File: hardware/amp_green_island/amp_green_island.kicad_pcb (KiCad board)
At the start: 4 copper layers, 100 x 100 mm, 39 parts, among them J501 input, J502 output, J503 Conn_01x04_Pin, U101 OP27, U102 TL072

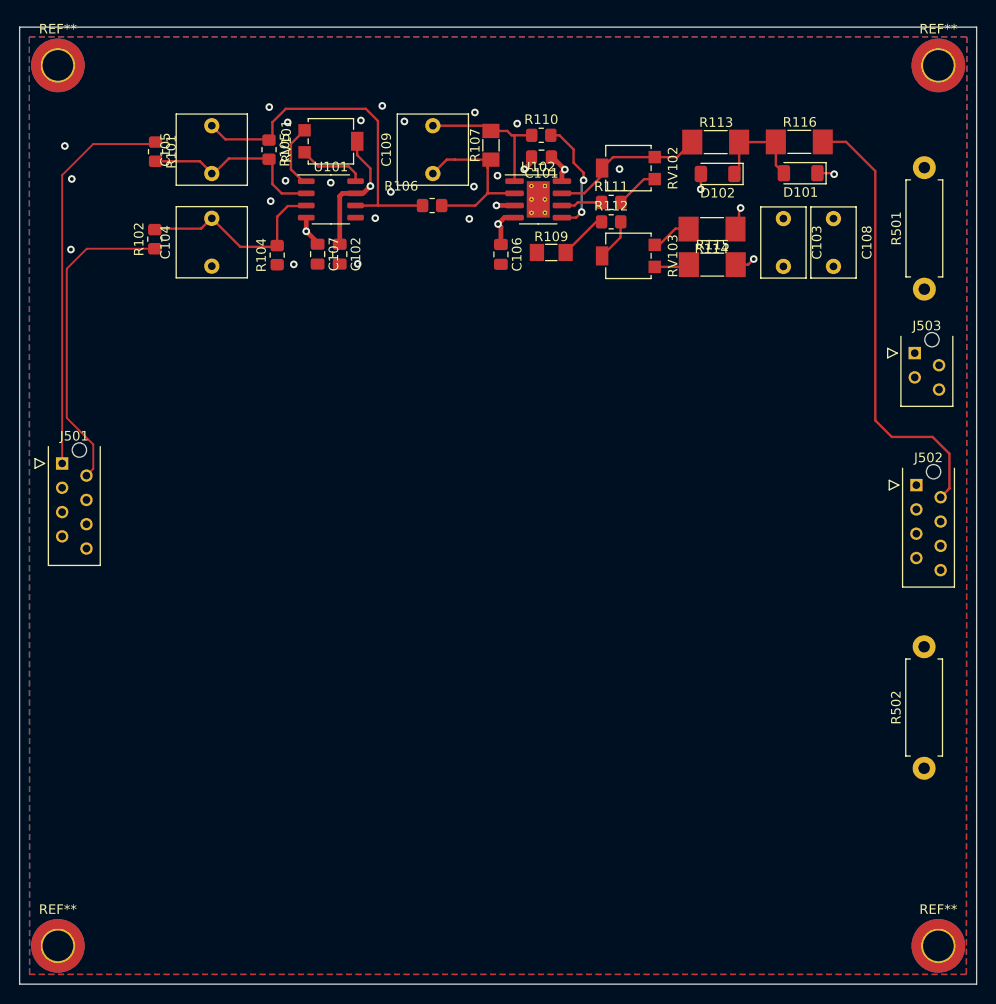
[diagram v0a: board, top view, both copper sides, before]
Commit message: amp_green_island: add all 4 channels to schematic
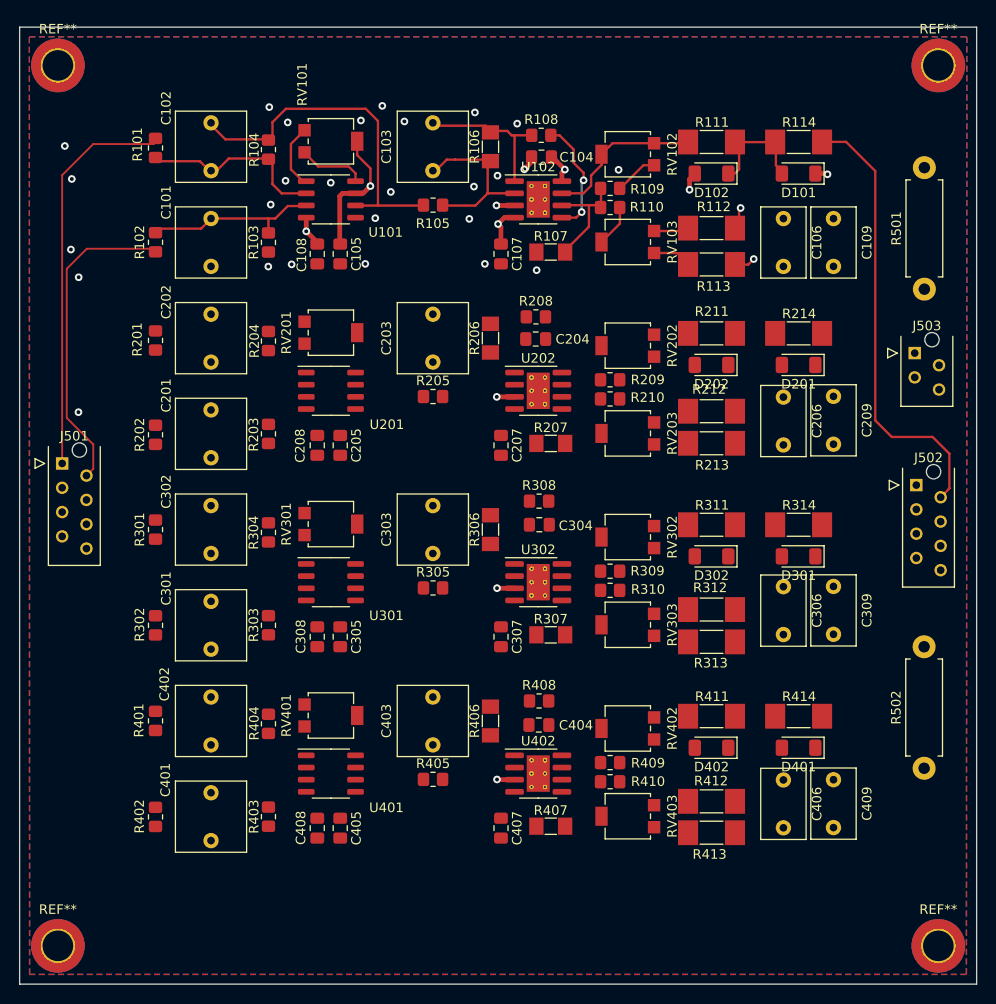
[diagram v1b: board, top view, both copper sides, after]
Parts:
- added C201: 1u, Capacitor_THT:C_Rect_L7.2mm_W7.2mm_P5.00mm_FKS2_FKP2_MKS2_MKP2, F.Cu at (120.0, 95.0)
- added C202: 1u, Capacitor_THT:C_Rect_L7.2mm_W7.2mm_P5.00mm_FKS2_FKP2_MKS2_MKP2, F.Cu at (120.0, 85.0)
- added C203: 1u, Capacitor_THT:C_Rect_L7.2mm_W7.2mm_P5.00mm_FKS2_FKP2_MKS2_MKP2, F.Cu at (143.2, 85.0)
- added C204: 100n, Capacitor_SMD:C_0805_2012Metric_Pad1.18x1.45mm_HandSolder, F.Cu at (153.9, 82.6)
- added C205: 100n, Capacitor_SMD:C_0805_2012Metric_Pad1.18x1.45mm_HandSolder, F.Cu at (133.5, 93.7)
- added C206: 100n, Capacitor_THT:C_Rect_L7.2mm_W4.5mm_P5.00mm_FKS2_FKP2_MKS2_MKP2, F.Cu at (179.8, 88.7)
- added C207: 100n, Capacitor_SMD:C_0805_2012Metric_Pad1.18x1.45mm_HandSolder, F.Cu at (150.3, 93.7)
- added C208: 100n, Capacitor_SMD:C_0805_2012Metric_Pad1.18x1.45mm_HandSolder, F.Cu at (131.1, 93.7)
- added C209: 100n, Capacitor_THT:C_Rect_L7.2mm_W4.5mm_P5.00mm_FKS2_FKP2_MKS2_MKP2, F.Cu at (185.0, 88.6)
- added C301: 1u, Capacitor_THT:C_Rect_L7.2mm_W7.2mm_P5.00mm_FKS2_FKP2_MKS2_MKP2, F.Cu at (120.0, 115.0)
- added C302: 1u, Capacitor_THT:C_Rect_L7.2mm_W7.2mm_P5.00mm_FKS2_FKP2_MKS2_MKP2, F.Cu at (120.0, 105.0)
- added C303: 1u, Capacitor_THT:C_Rect_L7.2mm_W7.2mm_P5.00mm_FKS2_FKP2_MKS2_MKP2, F.Cu at (143.2, 105.0)
- added C304: 100n, Capacitor_SMD:C_0805_2012Metric_Pad1.18x1.45mm_HandSolder, F.Cu at (154.3, 102.0)
- added C305: 100n, Capacitor_SMD:C_0805_2012Metric_Pad1.18x1.45mm_HandSolder, F.Cu at (133.5, 113.7)
- added C306: 100n, Capacitor_THT:C_Rect_L7.2mm_W4.5mm_P5.00mm_FKS2_FKP2_MKS2_MKP2, F.Cu at (179.8, 108.5)
- added C307: 100n, Capacitor_SMD:C_0805_2012Metric_Pad1.18x1.45mm_HandSolder, F.Cu at (150.3, 113.7)
- added C308: 100n, Capacitor_SMD:C_0805_2012Metric_Pad1.18x1.45mm_HandSolder, F.Cu at (131.1, 113.7)
- added C309: 100n, Capacitor_THT:C_Rect_L7.2mm_W4.5mm_P5.00mm_FKS2_FKP2_MKS2_MKP2, F.Cu at (185.0, 108.4)
- added C401: 1u, Capacitor_THT:C_Rect_L7.2mm_W7.2mm_P5.00mm_FKS2_FKP2_MKS2_MKP2, F.Cu at (120.0, 135.0)
- added C402: 1u, Capacitor_THT:C_Rect_L7.2mm_W7.2mm_P5.00mm_FKS2_FKP2_MKS2_MKP2, F.Cu at (120.0, 125.0)
- added C403: 1u, Capacitor_THT:C_Rect_L7.2mm_W7.2mm_P5.00mm_FKS2_FKP2_MKS2_MKP2, F.Cu at (143.2, 125.0)
- added C404: 100n, Capacitor_SMD:C_0805_2012Metric_Pad1.18x1.45mm_HandSolder, F.Cu at (154.3, 122.9)
- added C405: 100n, Capacitor_SMD:C_0805_2012Metric_Pad1.18x1.45mm_HandSolder, F.Cu at (133.5, 133.7)
- added C406: 100n, Capacitor_THT:C_Rect_L7.2mm_W4.5mm_P5.00mm_FKS2_FKP2_MKS2_MKP2, F.Cu at (179.8, 128.7)
- added C407: 100n, Capacitor_SMD:C_0805_2012Metric_Pad1.18x1.45mm_HandSolder, F.Cu at (150.3, 133.7)
- added C408: 100n, Capacitor_SMD:C_0805_2012Metric_Pad1.18x1.45mm_HandSolder, F.Cu at (131.1, 133.7)
- added C409: 100n, Capacitor_THT:C_Rect_L7.2mm_W4.5mm_P5.00mm_FKS2_FKP2_MKS2_MKP2, F.Cu at (185.0, 128.6)
- added D201: LL4148, Diode_SMD:D_MiniMELF, F.Cu at (181.4, 85.3)
- added D202: LL4148, Diode_SMD:D_MiniMELF, F.Cu at (172.3, 85.3)
- added D301: LL4148, Diode_SMD:D_MiniMELF, F.Cu at (181.4, 105.3)
- added D302: LL4148, Diode_SMD:D_MiniMELF, F.Cu at (172.3, 105.3)
- added D401: LL4148, Diode_SMD:D_MiniMELF, F.Cu at (181.4, 125.3)
- added D402: LL4148, Diode_SMD:D_MiniMELF, F.Cu at (172.3, 125.3)
- added R201: 10k, Resistor_SMD:R_0805_2012Metric_Pad1.20x1.40mm_HandSolder, F.Cu at (114.2, 82.7)
- added R202: 10k, Resistor_SMD:R_0805_2012Metric_Pad1.20x1.40mm_HandSolder, F.Cu at (114.2, 92.6)
- added R203: 100k, Resistor_SMD:R_0805_2012Metric_Pad1.20x1.40mm_HandSolder, F.Cu at (126.0, 92.5)
- added R204: 100k, Resistor_SMD:R_0805_2012Metric_Pad1.20x1.40mm_HandSolder, F.Cu at (126.0, 82.8)
- added R205: 1k, Resistor_SMD:R_0805_2012Metric_Pad1.20x1.40mm_HandSolder, F.Cu at (143.2, 88.6)
- added R206: 200k, Resistor_SMD:R_MiniMELF_MMA-0204, F.Cu at (149.2, 82.5)
- added R207: 3k3, Resistor_SMD:R_MiniMELF_MMA-0204, F.Cu at (155.5, 93.5)
- added R208: 1k, Resistor_SMD:R_0805_2012Metric_Pad1.20x1.40mm_HandSolder, F.Cu at (153.9, 80.3)
- added R209: 5k6, Resistor_SMD:R_0805_2012Metric_Pad1.20x1.40mm_HandSolder, F.Cu at (161.7, 86.8)
- added R210: 82k, Resistor_SMD:R_0805_2012Metric_Pad1.20x1.40mm_HandSolder, F.Cu at (161.7, 88.8)
- added R211: 470, Resistor_SMD:R_MELF_MMB-0207, F.Cu at (172.3, 82.0)
- added R212: 33k, Resistor_SMD:R_MELF_MMB-0207, F.Cu at (172.3, 90.1)
- added R213: 33k, Resistor_SMD:R_MELF_MMB-0207, F.Cu at (172.3, 93.5)
- added R214: 470, Resistor_SMD:R_MELF_MMB-0207, F.Cu at (181.4, 82.0)
- added R301: 10k, Resistor_SMD:R_0805_2012Metric_Pad1.20x1.40mm_HandSolder, F.Cu at (114.2, 102.5)
- added R302: 10k, Resistor_SMD:R_0805_2012Metric_Pad1.20x1.40mm_HandSolder, F.Cu at (114.2, 112.5)
- added R303: 100k, Resistor_SMD:R_0805_2012Metric_Pad1.20x1.40mm_HandSolder, F.Cu at (126.0, 112.5)
- added R304: 100k, Resistor_SMD:R_0805_2012Metric_Pad1.20x1.40mm_HandSolder, F.Cu at (126.0, 102.8)
- added R305: 1k, Resistor_SMD:R_0805_2012Metric_Pad1.20x1.40mm_HandSolder, F.Cu at (143.2, 108.6)
- added R306: 200k, Resistor_SMD:R_MiniMELF_MMA-0204, F.Cu at (149.2, 102.5)
- added R307: 3k3, Resistor_SMD:R_MiniMELF_MMA-0204, F.Cu at (155.5, 113.5)
- added R308: 1k, Resistor_SMD:R_0805_2012Metric_Pad1.20x1.40mm_HandSolder, F.Cu at (154.3, 99.5)
- added R309: 5k6, Resistor_SMD:R_0805_2012Metric_Pad1.20x1.40mm_HandSolder, F.Cu at (161.7, 106.8)
- added R310: 82k, Resistor_SMD:R_0805_2012Metric_Pad1.20x1.40mm_HandSolder, F.Cu at (161.7, 108.8)
- added R311: 470, Resistor_SMD:R_MELF_MMB-0207, F.Cu at (172.3, 102.0)
- added R312: 33k, Resistor_SMD:R_MELF_MMB-0207, F.Cu at (172.3, 110.9)
- added R313: 33k, Resistor_SMD:R_MELF_MMB-0207, F.Cu at (172.3, 114.2)
- added R314: 470, Resistor_SMD:R_MELF_MMB-0207, F.Cu at (181.4, 102.0)
- added R401: 10k, Resistor_SMD:R_0805_2012Metric_Pad1.20x1.40mm_HandSolder, F.Cu at (114.2, 122.5)
- added R402: 10k, Resistor_SMD:R_0805_2012Metric_Pad1.20x1.40mm_HandSolder, F.Cu at (114.2, 132.5)
- added R403: 100k, Resistor_SMD:R_0805_2012Metric_Pad1.20x1.40mm_HandSolder, F.Cu at (126.0, 132.5)
- added R404: 100k, Resistor_SMD:R_0805_2012Metric_Pad1.20x1.40mm_HandSolder, F.Cu at (126.0, 122.8)
- added R405: 1k, Resistor_SMD:R_0805_2012Metric_Pad1.20x1.40mm_HandSolder, F.Cu at (143.2, 128.6)
- added R406: 200k, Resistor_SMD:R_MiniMELF_MMA-0204, F.Cu at (149.2, 122.5)
- added R407: 3k3, Resistor_SMD:R_MiniMELF_MMA-0204, F.Cu at (155.5, 133.5)
- added R408: 1k, Resistor_SMD:R_0805_2012Metric_Pad1.20x1.40mm_HandSolder, F.Cu at (154.3, 120.4)
- added R409: 5k6, Resistor_SMD:R_0805_2012Metric_Pad1.20x1.40mm_HandSolder, F.Cu at (161.7, 126.8)
- added R410: 82k, Resistor_SMD:R_0805_2012Metric_Pad1.20x1.40mm_HandSolder, F.Cu at (161.7, 128.8)
- added R411: 470, Resistor_SMD:R_MELF_MMB-0207, F.Cu at (172.3, 122.0)
- added R412: 33k, Resistor_SMD:R_MELF_MMB-0207, F.Cu at (172.3, 130.9)
- added R413: 33k, Resistor_SMD:R_MELF_MMB-0207, F.Cu at (172.3, 134.2)
- added R414: 470, Resistor_SMD:R_MELF_MMB-0207, F.Cu at (181.4, 122.0)
- added RV201: 10k, Potentiometer_SMD:Potentiometer_Bourns_3314G_Vertical, F.Cu at (132.5, 81.9)
- added RV202: 50k, Potentiometer_SMD:Potentiometer_Bourns_3314G_Vertical, F.Cu at (163.6, 83.3)
- added RV203: 5k, Potentiometer_SMD:Potentiometer_Bourns_3314G_Vertical, F.Cu at (163.6, 92.5)
- added RV301: 10k, Potentiometer_SMD:Potentiometer_Bourns_3314G_Vertical, F.Cu at (132.5, 101.9)
- added RV302: 50k, Potentiometer_SMD:Potentiometer_Bourns_3314G_Vertical, F.Cu at (163.6, 103.3)
- added RV303: 5k, Potentiometer_SMD:Potentiometer_Bourns_3314G_Vertical, F.Cu at (163.6, 112.5)
- added RV401: 10k, Potentiometer_SMD:Potentiometer_Bourns_3314G_Vertical, F.Cu at (132.5, 121.9)
- added RV402: 50k, Potentiometer_SMD:Potentiometer_Bourns_3314G_Vertical, F.Cu at (163.6, 123.3)
- added RV403: 5k, Potentiometer_SMD:Potentiometer_Bourns_3314G_Vertical, F.Cu at (163.6, 132.5)
- added U201: OP27, Package_SO:SO-8_3.9x4.9mm_P1.27mm, F.Cu at (132.5, 88.0)
- added U202: TL072, Package_SO:SOIC-8-1EP_3.9x4.9mm_P1.27mm_EP2.41x3.81mm_ThermalVias, F.Cu at (154.2, 88.0)
- added U301: OP27, Package_SO:SO-8_3.9x4.9mm_P1.27mm, F.Cu at (132.5, 108.0)
- added U302: TL072, Package_SO:SOIC-8-1EP_3.9x4.9mm_P1.27mm_EP2.41x3.81mm_ThermalVias, F.Cu at (154.2, 108.0)
- added U401: OP27, Package_SO:SO-8_3.9x4.9mm_P1.27mm, F.Cu at (132.5, 128.0)
- added U402: TL072, Package_SO:SOIC-8-1EP_3.9x4.9mm_P1.27mm_EP2.41x3.81mm_ThermalVias, F.Cu at (154.2, 128.0)
- moved R103 1.61 mm to (126.0, 72.5)
- moved R110 1.50 mm to (161.7, 68.8)
- moved R109 1.47 mm to (161.7, 66.8)
- moved RV102 1.45 mm to (163.6, 63.3)
- moved RV103 1.45 mm to (163.6, 72.5)
- moved D102 0.64 mm to (172.3, 65.3)
- moved R111 0.44 mm to (172.3, 62.0)
- moved R101 0.39 mm to (114.2, 62.6)
- moved R102 0.33 mm to (114.2, 72.5)
- moved C102 0.31 mm to (120.0, 65.0)
- moved C103 0.30 mm to (143.2, 65.0)
- moved D101 0.21 mm to (181.4, 65.3)
- moved R106 0.16 mm to (149.2, 62.5)
- moved R112 0.12 mm to (172.3, 71.0)
- moved R105 0.11 mm to (143.2, 68.6)
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- renumbered C104 to C101, C105 to C102, C109 to C103, C101 to C104, C102 to C105, C103 to C106, C106 to C107, C107 to C108, C108 to C109, R104 to R103, R105 to R104, R106 to R105, R107 to R106, R109 to R107, R110 to R108, R111 to R109, R112 to R110, R113 to R111, R114 to R112, R115 to R113, R116 to R114
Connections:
- J501 pad 3: unconnected-(J501-Pin_3-Pad3) -> in2_-
- J501 pad 4: unconnected-(J501-Pin_4-Pad4) -> in2_+
- J501 pad 5: unconnected-(J501-Pin_5-Pad5) -> in3_-
- J501 pad 6: unconnected-(J501-Pin_6-Pad6) -> in3_+
- J501 pad 7: unconnected-(J501-Pin_7-Pad7) -> in4_-
- J501 pad 8: unconnected-(J501-Pin_8-Pad8) -> in4_+
- J502 pad 4: unconnected-(J502-Pin_4-Pad4) -> out2
- J502 pad 6: unconnected-(J502-Pin_6-Pad6) -> out3
- J502 pad 8: unconnected-(J502-Pin_8-Pad8) -> out4
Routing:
- net GND: track 3.77 -> 9.30 mm, vias 23 -> 31
- net Net-(U102B--): track 9.36 -> 12.2 mm
- net Net-(U101-+): track 21.1 -> 18.4 mm
- net Net-(R112-Pad2): track 4.61 -> 3.68 mm
- net Net-(R111-Pad1): track 16.3 -> 17.1 mm
- net -12V: track 131.1 -> 131.8 mm

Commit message: green_island: pcb routing done
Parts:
- added C501: 220u, Capacitor_SMD:C_Elec_8x10.2, F.Cu at (163.8, 142.3)
- added C502: 220u, Capacitor_SMD:C_Elec_8x10.2, F.Cu at (182.5, 142.3)
- moved J502 2.46 mm to (193.7, 95.4)
- moved R308 1.78 mm to (154.5, 101.3)
- moved C304 1.62 mm to (154.5, 103.6), turned to 180 degrees
- moved C309 1.55 mm to (185.0, 110.0)
- moved C306 1.53 mm to (179.8, 110.0)
- moved C209 1.42 mm to (185.0, 90.0)
- moved C409 1.36 mm to (185.0, 130.0)
- moved C206 1.34 mm to (179.8, 90.0)
- moved C406 1.34 mm to (179.8, 130.0)
- moved R213 1.32 mm to (172.3, 94.8)
- moved C204 1.16 mm to (154.5, 83.6), turned to 180 degrees
- moved R208 1.16 mm to (154.5, 81.3)
- moved R408 0.92 mm to (154.5, 121.3)
- moved R212 0.87 mm to (172.3, 91.0)
- moved C404 0.72 mm to (154.5, 123.6), turned to 180 degrees
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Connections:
- J502 pad 1: GND -> out1
- J502 pad 2: out1 -> GND
- J502 pad 3: GND -> out2
- J502 pad 4: out2 -> GND
- J502 pad 5: GND -> out3
- J502 pad 6: out3 -> GND
- J502 pad 7: GND -> out4
- J502 pad 8: out4 -> GND
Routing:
- net +12V: track 119.1 -> 472.2 mm, vias 4 -> 18
- net -12V: track 131.8 -> 473.0 mm, vias 4 -> 18
- net Net-(C202-Pad2): track 0.00 -> 37.8 mm
- net Net-(C302-Pad2): track 0.00 -> 37.4 mm
- net Net-(C402-Pad2): track 0.00 -> 37.1 mm
- net in4_+: track 0.00 -> 31.8 mm
- net in2_-: track 0.00 -> 27.1 mm
- net in4_-: track 0.00 -> 25.7 mm
- net out4: track 0.00 -> 25.4 mm
- net out2: track 0.00 -> 20.6 mm
- net Net-(U301--): track 0.00 -> 20.6 mm
- net Net-(U201--): track 0.00 -> 19.9 mm
- net Net-(U401--): track 0.00 -> 19.7 mm
- net Net-(U301-+): track 0.00 -> 19.6 mm
- net Net-(U401-+): track 0.00 -> 19.3 mm
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- added copper zone on In2.Cu, net GND

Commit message: amp_green_island: pcb verified
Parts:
- added D501: LED, LED_SMD:LED_0805_2012Metric_Pad1.15x1.40mm_HandSolder, F.Cu at (118.7, 145.7)
- added D502: LED, LED_SMD:LED_0805_2012Metric_Pad1.15x1.40mm_HandSolder, F.Cu at (113.9, 145.7)
- added R503: 100k, Resistor_SMD:R_0805_2012Metric_Pad1.20x1.40mm_HandSolder, F.Cu at (118.7, 142.1)
- added R504: 100k, Resistor_SMD:R_0805_2012Metric_Pad1.20x1.40mm_HandSolder, F.Cu at (113.9, 142.1)
- U102, U202, U302, U402: footprint Package_SO:SOIC-8-1EP_3.9x4.9mm_P1.27mm_EP2.41x3.81mm_ThermalVias -> Package_SO:SO-8_3.9x4.9mm_P1.27mm
- moved J502 0.21 mm to (193.7, 95.6)
- moved J503 0.17 mm to (193.7, 84.1)
- moved J501 0.06 mm to (104.5, 95.6)
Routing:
- net -12V: track 473.0 -> 563.5 mm, vias 18 -> 19
- net +12V: track 472.2 -> 530.4 mm, vias 18 -> 19
- net Net-(D501-A): track 0.00 -> 3.67 mm
- net Net-(D502-K): track 0.00 -> 3.61 mm
- net Net-(C203-Pad2): track 15.6 -> 16.6 mm
- net Net-(C202-Pad2): track 37.8 -> 36.9 mm
- net Net-(C303-Pad2): track 15.6 -> 16.4 mm
- net Net-(U402B--): track 12.0 -> 12.8 mm
- net in1_+: track 33.1 -> 32.3 mm
- net Net-(C403-Pad2): track 15.6 -> 16.3 mm
- net Net-(U302B--): track 12.0 -> 12.7 mm
- net out1: track 38.9 -> 38.2 mm
- net out4: track 25.4 -> 24.7 mm
- net Net-(C302-Pad2): track 37.4 -> 36.8 mm
- net Net-(U102B--): track 12.2 -> 12.8 mm
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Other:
- board text added: "-12V +12V"
- board text added: "0V trim"
- board text added: "gain"
- board text added: "geophone amplifier - green isl. rev 1 https://github.com/rodan/rumble Petre Rodan 2023.09"
- board text added: "in1 + in2 + in3 + in4 +"
- board text added: "in1 - in2 - in3 - in4 -"
- board text added: "input"
- board text added: "offset"
- board text added: "out1 out2 out3 out4"
- board text added: "output"
